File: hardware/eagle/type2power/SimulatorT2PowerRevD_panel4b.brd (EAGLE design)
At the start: 99.1 x 99.1 mm, 49 parts

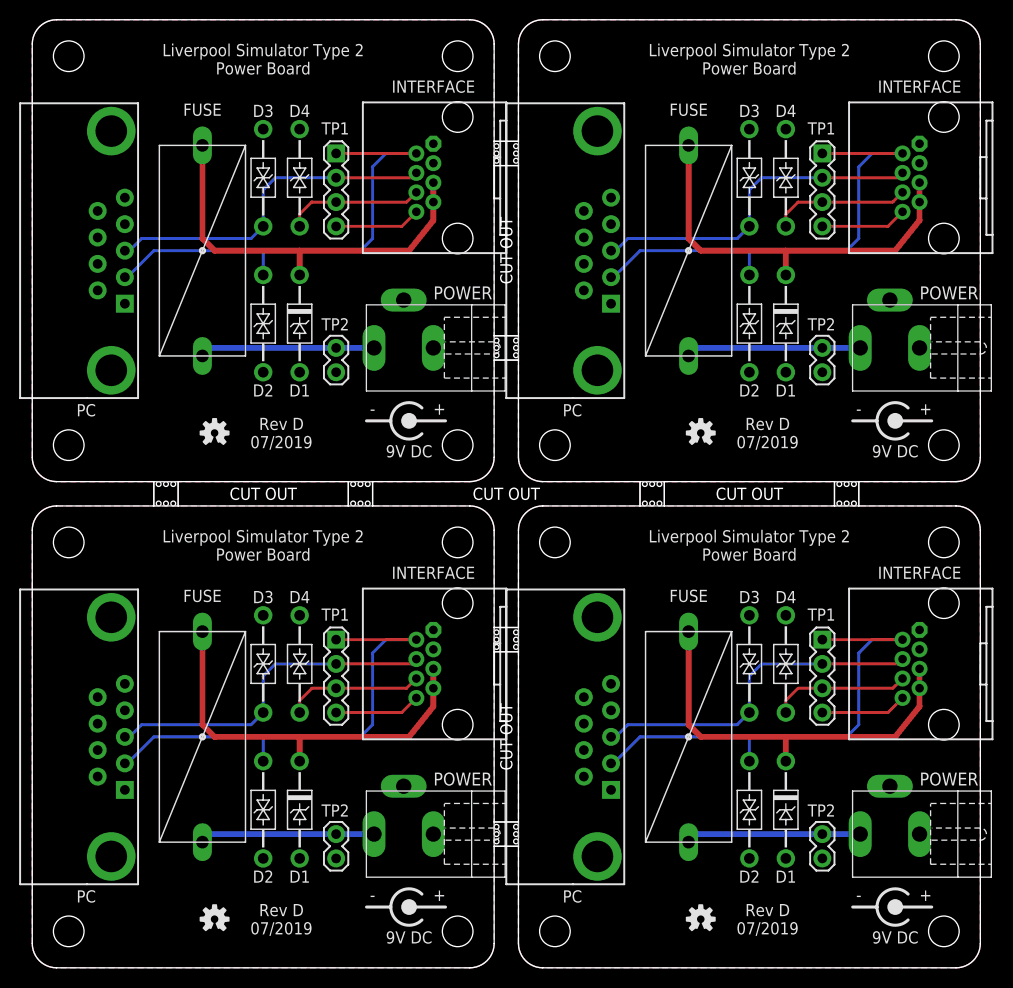
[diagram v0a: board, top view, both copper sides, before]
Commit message: Wider 5mm break-offs
Issues with JLPCB rejecting panelised boards with 2.5mm stamp hole
break-off tabs. Increased tab width to 5mm on all panelised boards.
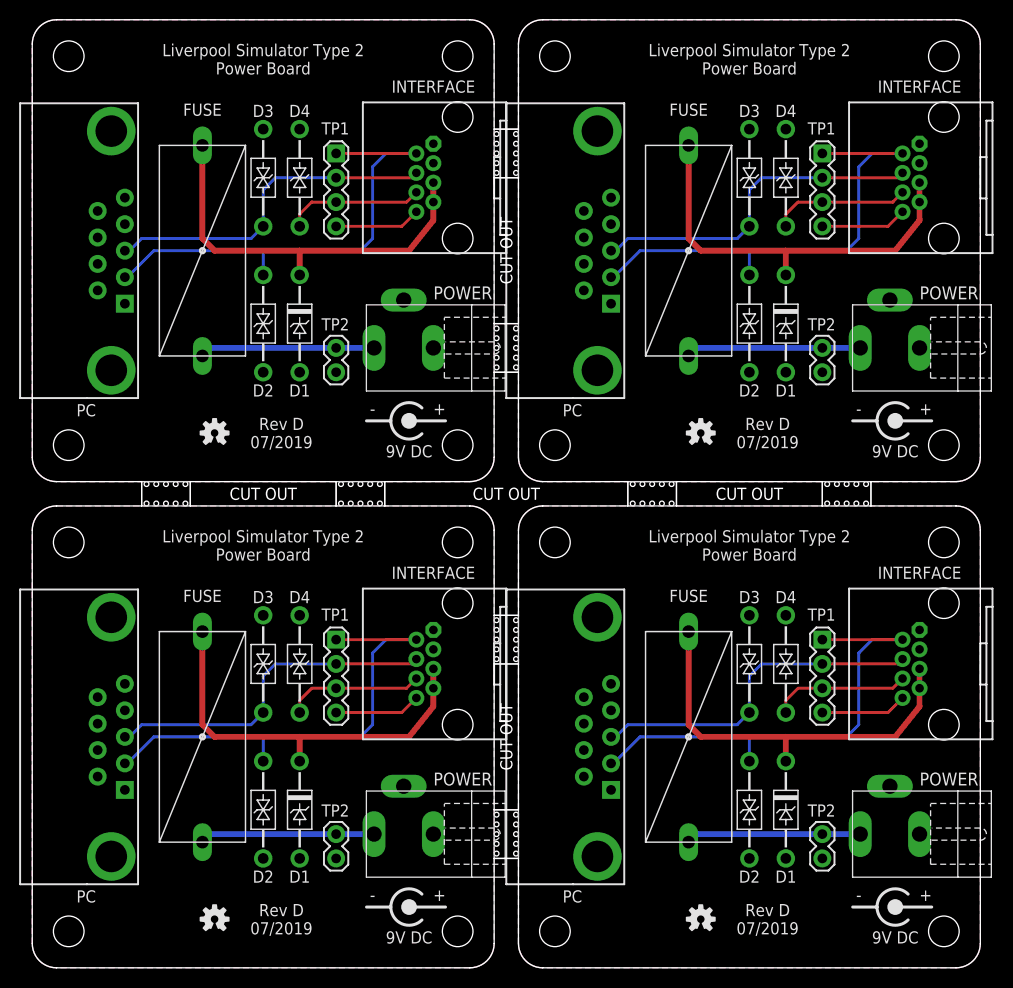
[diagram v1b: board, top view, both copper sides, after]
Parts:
- removed E$1: (no value), AIC_Custom:OUTLINE_PANEL_4
- added E$2: (no value), AIC_Custom:OUTLINE_PANEL_4_5MM
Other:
- outline, holes or cut-outs redrawn
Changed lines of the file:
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@@
 <text x="26.035" y="5.08" size="1.27" layer="21" font="vector" align="center">Rev D
 07/2019</text>
-<dimension x1="49.53" y1="48.26" x2="49.53" y2="0" x3="55.88000625" y3="24.13" textsize="1.778" layer="47"/>
 <text x="27.94" y="10.16" size="1.27" layer="125" rot="R180" align="bottom-center">D1</text>
 <text x="24.13" y="10.16" size="1.27" layer="125" rot="R180" align="bottom-center">D2</text>
@@
 <attribute name="NAME1" value="D4" x="78.74" y="88.9" size="1.27" layer="25" font="vector" align="bottom-center"/>
 </element>
-<element name="E$1" library="AIC_Custom" package="OUTLINE_PANEL_4" value="" x="0" y="0"/>
+<element name="E$2" library="AIC_Custom" package="OUTLINE_PANEL_4_5MM" value="" x="0" y="0"/>
 </elements>
 <signals>
